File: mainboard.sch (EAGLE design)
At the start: 133 parts, among them X1 FH12-24S-0.5SH, X3 87438-02

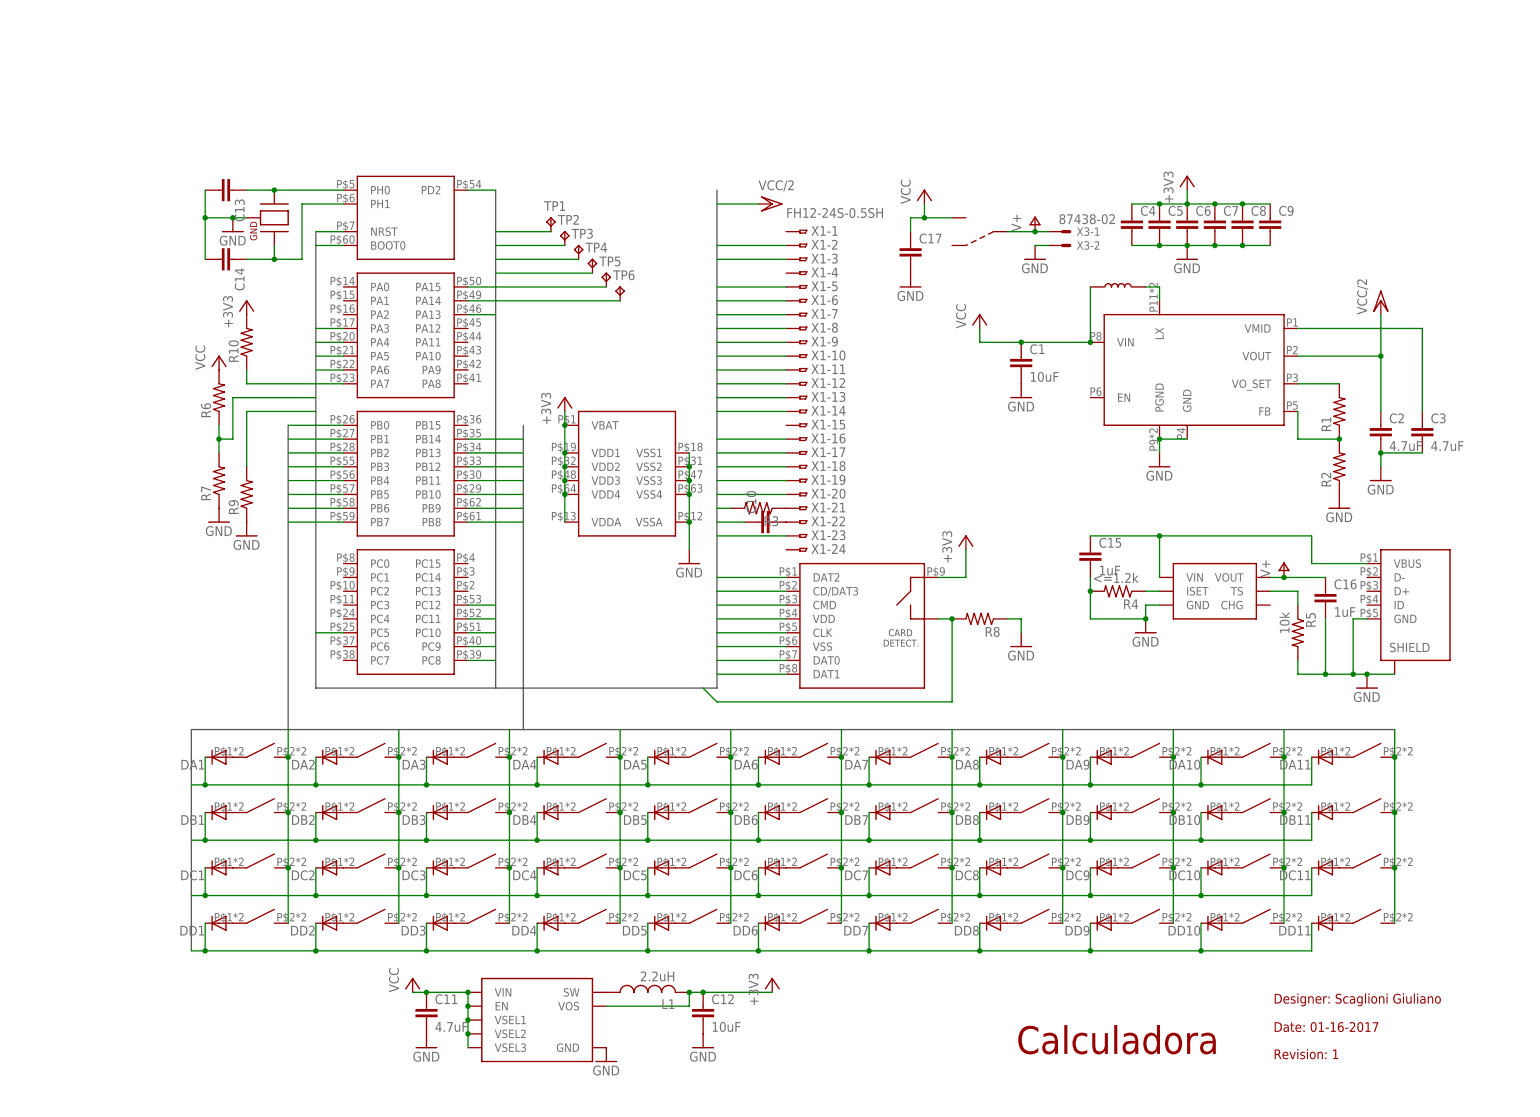
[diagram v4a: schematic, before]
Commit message: [FIX] Missing EN connection in STOD1317BTPUR
Conected EN Pin in STOD1317BTPUR to 3v3
Added 0402 led for tests.
Moved components from bga8 chip to allow visual inspection of soldering.
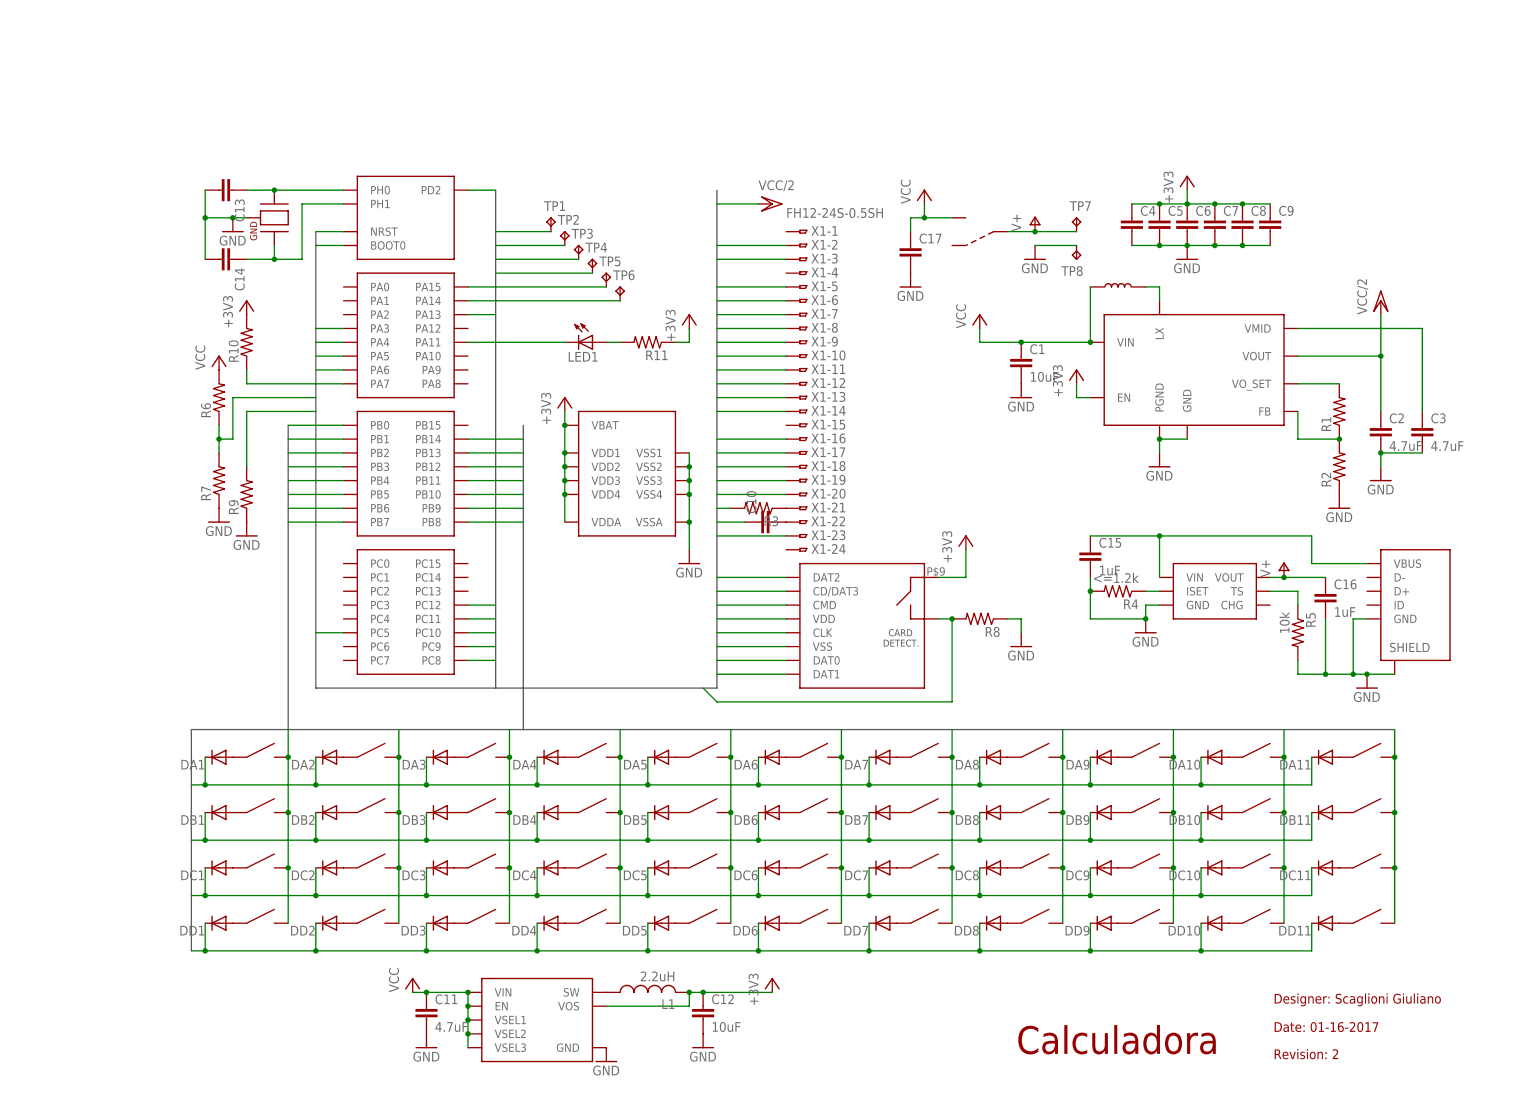
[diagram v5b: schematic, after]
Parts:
- removed X3: 87438-02, con-molex:87438-02
- added LED1: (no value), eagle-ltspice:LED_ESML0603
- added R11: (no value), resistor:R-US_R0402
- added TP7, TP8: TPTP20SQ, testpad:TPTP20SQ
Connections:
- new net N$57: LED1.A, R11.2
- new net N$58: LED1.C, U$1G$2.PA11
- net +3V3: now also R11.1, U$4.EN
- net GND: now also TP8.TP; no longer X3-2.S
- net V+: now also TP7.TP; no longer X3-1.S
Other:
- note added: "Revision: 2"
- note removed: "Revision: 1"
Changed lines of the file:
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@@
 <setting verticaltext="up"/>
 </settings>
-<grid distance="0.1" unitdist="mm" unit="mm" style="lines" multiple="1" display="no" altdistance="0.01" altunitdist="inch" altunit="inch"/>
+<grid distance="0.1" unitdist="inch" unit="inch" style="lines" multiple="1" display="no" altdistance="0.01" altunitdist="inch" altunit="inch"/>
 <layers>
 <layer number="1" name="Top" color="4" fill="1" visible="no" active="no"/>
@@
 <part name="DD10" library="diode" deviceset="DIODE-" device="SOD523"/>
 <part name="DD11" library="diode" deviceset="DIODE-" device="SOD523"/>
-<part name="X3" library="con-molex" deviceset="87438-02" device=""/>
 <part name="U$6" library="lib" deviceset="TPS627431YFPR" device=""/>
 <part name="P+5" library="supply1" deviceset="VCC" device=""/>
@@
 <part name="GND16" library="supply1" deviceset="GND" device=""/>
 <part name="GND17" library="supply1" deviceset="GND" device=""/>
+<part name="+3V6" library="supply1" deviceset="+3V3" device=""/>
+<part name="LED1" library="eagle-ltspice" deviceset="LED_E" device="SML0603"/>
+<part name="R11" library="resistor" deviceset="R-US_" device="R0402"/>
+<part name="+3V7" library="supply1" deviceset="+3V3" device=""/>
+<part name="TP7" library="testpad" deviceset="TP" device="TP20SQ"/>
+<part name="TP8" library="testpad" deviceset="TP" device="TP20SQ"/>
 </parts>
 <sheets>
@@
 <text x="216.5" y="20.8" size="1.778" layer="94">Designer: Scaglioni Giuliano</text>
 <text x="216.5" y="15.6" size="1.778" layer="94">Date: 01-16-2017</text>
-<text x="216.5" y="10.6" size="1.778" layer="94">Revision: 1</text>
+<text x="216.5" y="10.6" size="1.778" layer="94">Revision: 2</text>
 </plain>
 <instances>
@@
 <instance part="DD10" gate="G$1" x="205.74" y="35.56" rot="R180"/>
 <instance part="DD11" gate="G$1" x="226.06" y="35.56" rot="R180"/>
-<instance part="X3" gate="-1" x="177.8" y="162.56"/>
-<instance part="X3" gate="-2" x="177.8" y="160.02"/>
 <instance part="U$6" gate="G$1" x="81.28" y="17.78"/>
 <instance part="P+5" gate="VCC" x="58.42" y="25.4"/>
@@
 <instance part="GND16" gate="1" x="60.96" y="12.7"/>
 <instance part="GND17" gate="1" x="111.76" y="12.7"/>
+<instance part="+3V6" gate="G$1" x="180.34" y="137.16"/>
+<instance part="LED1" gate="G$1" x="91.44" y="142.24" rot="R270"/>
+<instance part="R11" gate="G$1" x="101.6" y="142.24" rot="R180"/>
+<instance part="+3V7" gate="G$1" x="109.22" y="147.32"/>
+<instance part="TP7" gate="G$1" x="180.34" y="165.1"/>
+<instance part="TP8" gate="G$1" x="180.34" y="157.48" rot="R180"/>
 </instances>
 <busses>
@@
 <segment>
 <pinref part="GND7" gate="1" pin="GND"/>
-<wire x1="175.26" y1="160.02" x2="172.72" y2="160.02" width="0.1524" layer="91"/>
-<pinref part="X3" gate="-2" pin="S"/>
+<pinref part="TP8" gate="G$1" pin="TP"/>
+<wire x1="172.72" y1="160.02" x2="180.34" y2="160.02" width="0.1524" layer="91"/>
 </segment>
 <segment>
@@
 <pinref part="R10" gate="G$1" pin="2"/>
 <pinref part="+3V5" gate="G$1" pin="+3V3"/>
+</segment>
+<segment>
+<pinref part="+3V6" gate="G$1" pin="+3V3"/>
+<pinref part="U$4" gate="G$1" pin="EN"/>
+<wire x1="180.34" y1="134.62" x2="180.34" y2="132.08" width="0.1524" layer="91"/>
+<wire x1="180.34" y1="132.08" x2="182.88" y2="132.08" width="0.1524" layer="91"/>
+</segment>
+<segment>
+<pinref part="R11" gate="G$1" pin="1"/>
+<pinref part="+3V7" gate="G$1" pin="+3V3"/>
+<wire x1="106.68" y1="142.24" x2="109.22" y2="142.24" width="0.1524" layer="91"/>
+<wire x1="109.22" y1="142.24" x2="109.22" y2="144.78" width="0.1524" layer="91"/>
 </segment>
 </net>
@@
 <segment>
 <pinref part="P+7" gate="1" pin="V+"/>
-<pinref part="X3" gate="-1" pin="S"/>
-<wire x1="172.72" y1="162.56" x2="175.26" y2="162.56" width="0.1524" layer="91"/>
 <pinref part="U$9" gate="G$1" pin="COM"/>
 <wire x1="167.64" y1="162.56" x2="172.72" y2="162.56" width="0.1524" layer="91"/>
 <junction x="172.72" y="162.56"/>
+<pinref part="TP7" gate="G$1" pin="TP"/>
+<wire x1="172.72" y1="162.56" x2="180.34" y2="162.56" width="0.1524" layer="91"/>
 </segment>
 </net>
@@
 </segment>
 </net>
+<net name="N$57" class="0">
+<segment>
+<pinref part="LED1" gate="G$1" pin="A"/>
+<pinref part="R11" gate="G$1" pin="2"/>
+<wire x1="93.98" y1="142.24" x2="96.52" y2="142.24" width="0.1524" layer="91"/>
+</segment>
+</net>
+<net name="N$58" class="0">
+<segment>
+<pinref part="LED1" gate="G$1" pin="C"/>
+<pinref part="U$1" gate="G$2" pin="PA11"/>
+<wire x1="86.36" y1="142.24" x2="68.58" y2="142.24" width="0.1524" layer="91"/>
+</segment>
+</net>
